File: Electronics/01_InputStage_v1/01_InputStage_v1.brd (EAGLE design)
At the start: 100 x 80 mm, 32 parts, among them J1 BARRIER_BLOCK-2PIN, J17 CONN_2X3_SMD, J2 BARRIER_BLOCK-2PIN, J3 BARRIER_BLOCK-2PIN, SW1 SWITCH_TABSSWITCH_TABS3, U1 XL4005-DEV, U2 DIODE_BIG

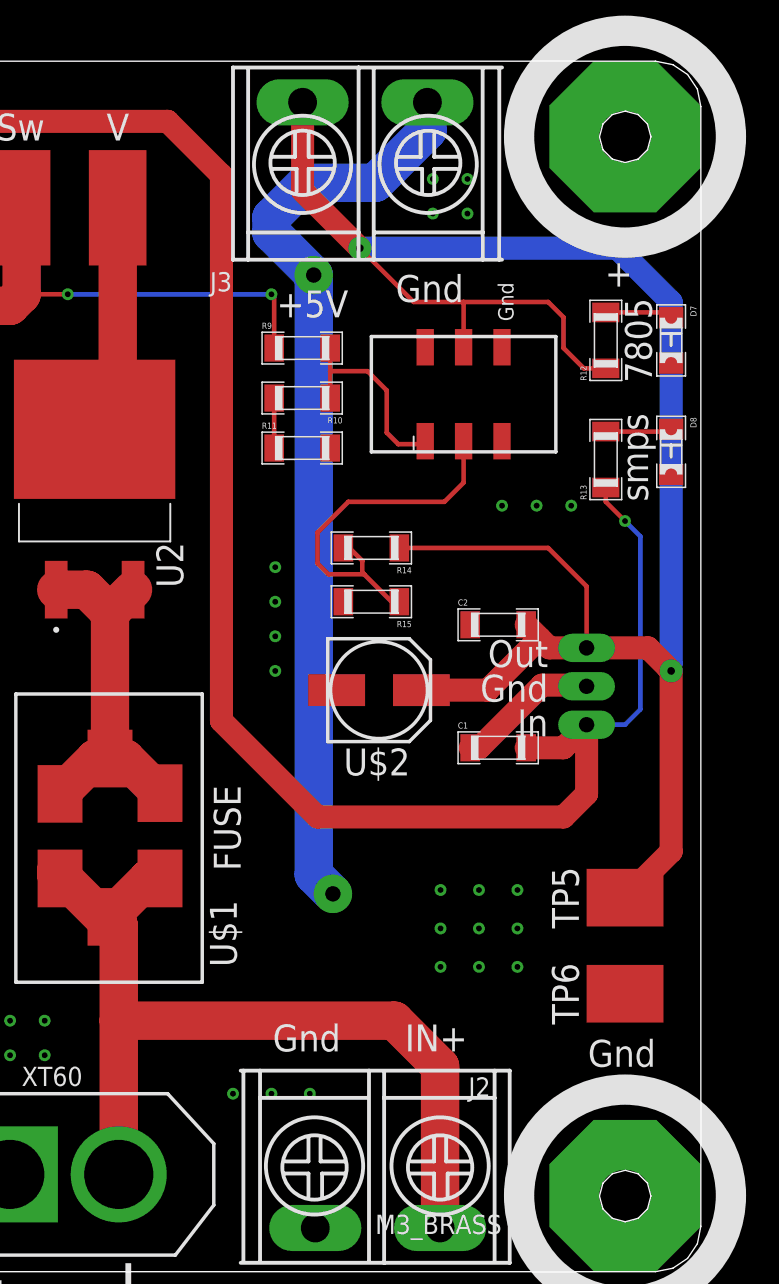
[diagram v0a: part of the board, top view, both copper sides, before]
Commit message: Input stage: Added PTC and moved some traces around
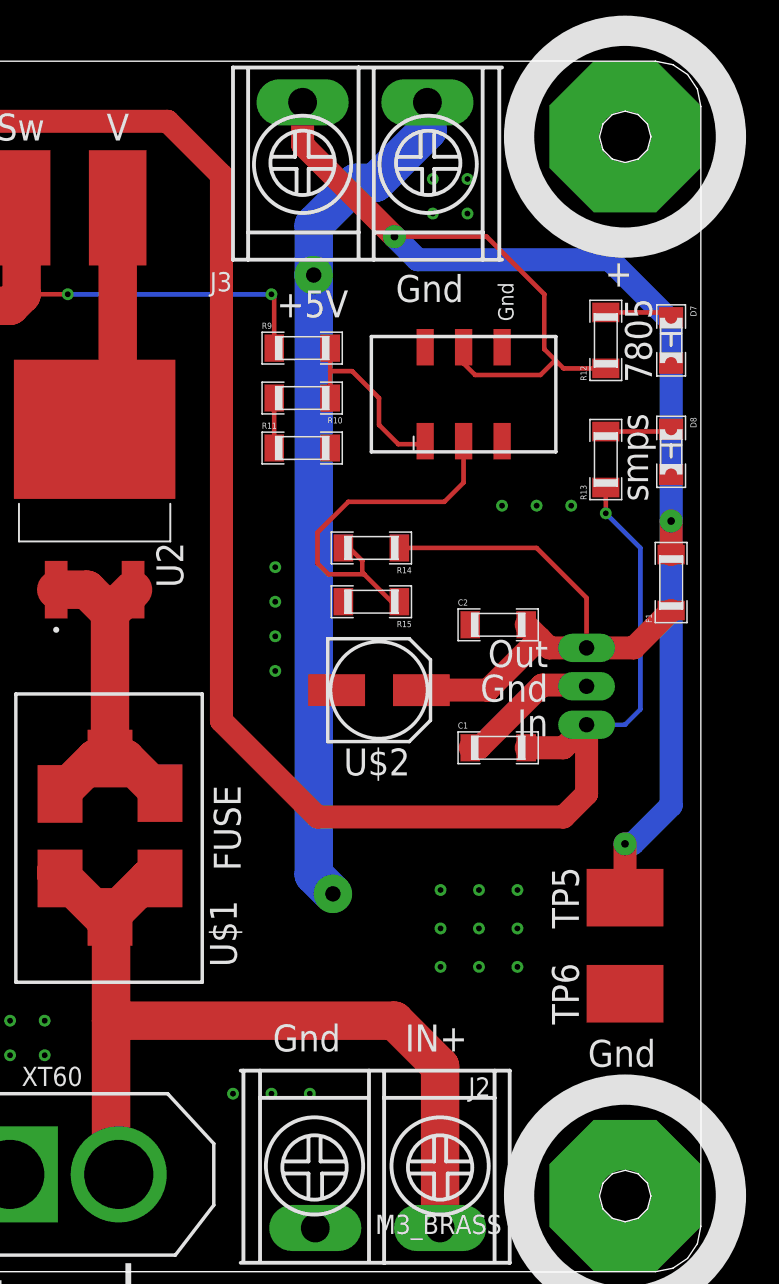
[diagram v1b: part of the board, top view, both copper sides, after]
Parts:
- added F1: PTCPTC_1206, Hippo-PS:1206
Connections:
- new net N: C2.2, F1.1, R14.1, U$2.+, U3.OUT
- net +5V: now also F1.2; no longer C2.2, R14.1, U$2.+, U3.OUT
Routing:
- net N: track 0.00 -> 37.5 mm
- net +5V: track 135.4 -> 101.4 mm, vias 2 -> 3
- net GND: track 98.6 -> 94.4 mm
- net IN+_SIG: track 13.3 -> 12.7 mm
- net IN+: track 60.2 -> 60.7 mm

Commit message: Change fuse holder to through-hole component
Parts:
- removed U$1: FUSE, Hippo-PS:FUSE
- added F2: FUSE_HOLDER_TH, Hippo-PS:FUSE_HOLDER_TH
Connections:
- net IN+: now also F2.1, F2.2; no longer U$1.P$1, U$1.P$2, U$1.P$3
- net N$1: now also F2.3, F2.4; no longer U$1.P$4, U$1.P$5, U$1.P$6
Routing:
- net N$1: track 24.5 -> 16.5 mm
- net IN+: track 60.7 -> 54.5 mm
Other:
- board text added: "hippo-pd input v1"
- board text removed: "hippo-ps input v1"
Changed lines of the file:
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@@
 <text x="156.972" y="46.99" size="1.524" layer="25" font="vector" ratio="15">word</text>
 <text x="104.902" y="81.026" size="1.016" layer="21" font="vector" ratio="14" rot="R90">Gnd</text>
-<text x="29.718" y="63.5" size="1.016" layer="21" font="vector" ratio="14" rot="R90">hippo-ps input v1</text>
-<text x="29.718" y="36.576" size="1.016" layer="21" font="vector" ratio="14" rot="R90">ek robotgrrl jul 10, `22</text>
+<text x="28.956" y="75.946" size="1.016" layer="21" font="vector" ratio="14" rot="SR270">hippo-pd input v1</text>
+<text x="28.702" y="52.832" size="1.016" layer="21" font="vector" ratio="14" rot="SR270">ek robotgrrl jul 10, `22</text>
 <text x="93.472" y="34.544" size="1.778" layer="21" font="vector" ratio="14" rot="R180">Gnd</text>
 <text x="101.854" y="34.544" size="1.778" layer="21" font="vector" ratio="14" rot="R180">IN+</text>
@@
 <attribute name="VALUE" x="72.39" y="30.48" size="1.27" layer="21" font="vector" ratio="14"/>
 </element>
-<element name="U$1" library="Hippo-PS" package="FUSE" value="FUSE" x="84.328" y="37.338" smashed="yes" rot="R90">
-<attribute name="NAME" x="86.614" y="38.354" size="1.778" layer="21" font="vector" ratio="14" rot="R90"/>
-<attribute name="VALUE" x="86.868" y="44.704" size="1.778" layer="21" font="vector" ratio="14" rot="R90"/>
-</element>
 <element name="TP1" library="Hippo-PS" package="TP" value="TP" x="34.798" y="36.322" smashed="yes">
 <attribute name="NAME" x="32.512" y="34.29" size="1.778" layer="25" font="vector" ratio="14" rot="R90"/>
@@
 <attribute name="VALUE" x="116.967" y="61.087" size="0.4064" layer="27" font="vector" rot="R90"/>
 </element>
+<element name="F2" library="Hippo-PS" package="FUSE_HOLDER_TH" value="FUSE_HOLDER_TH" x="75.438" y="41.91" smashed="yes" rot="R90">
+<attribute name="COPYRIGHT" value="Copyright (C) 2022 Ultra Librarian. All rights reserved." x="75.438" y="41.91" size="1.778" layer="27" rot="R90" display="off"/>
+<attribute name="DIGI-KEY_PART_NUMBER_1" value="36-3557-10-ND" x="75.438" y="41.91" size="1.778" layer="27" rot="R90" display="off"/>
+<attribute name="MANUFACTURER_PART_NUMBER" value="3557-10" x="75.438" y="41.91" size="1.778" layer="27" rot="R90" display="off"/>
+<attribute name="MFR_NAME" value="Keystone Electronics" x="75.438" y="41.91" size="1.778" layer="27" rot="R90" display="off"/>
+<attribute name="NAME" x="77.7748" y="45.3644" size="1.27" layer="27" ratio="6" rot="SR90"/>
+<attribute name="VALUE" x="77.5208" y="48.4378" size="1.27" layer="21" ratio="6" rot="SR90"/>
+</element>
 </elements>
 <signals>
@@
 <contactref element="U$5" pad="V+"/>
 <contactref element="J2" pad="P$1"/>
-<contactref element="U$1" pad="P$3"/>
-<contactref element="U$1" pad="P$2"/>
-<contactref element="U$1" pad="P$1"/>
-<wire x1="78.302" y1="34.798" x2="78.302" y2="25.146" width="2.54" layer="1"/>
+<wire x1="78.302" y1="25.146" x2="78.302" y2="34.798" width="2.54" layer="1"/>
 <wire x1="78.81" y1="24.638" x2="78.302" y2="25.146" width="2.54" layer="1"/>
-<wire x1="78.302" y1="34.798" x2="78.302" y2="41.586" width="2.54" layer="1"/>
-<wire x1="78.302" y1="41.586" x2="78.232" y2="41.656" width="2.54" layer="1"/>
-<wire x1="78.232" y1="41.656" x2="80.772" y2="44.196" width="2.54" layer="1"/>
-<wire x1="80.772" y1="44.196" x2="81.534" y2="44.196" width="2.54" layer="1"/>
-<wire x1="78.232" y1="41.656" x2="77.724" y2="41.656" width="2.54" layer="1"/>
-<wire x1="77.724" y1="41.656" x2="74.676" y2="44.704" width="2.54" layer="1"/>
-<wire x1="74.676" y1="44.704" x2="74.676" y2="44.45" width="2.54" layer="1"/>
-<wire x1="74.676" y1="44.45" x2="74.93" y2="44.196" width="2.54" layer="1"/>
 <wire x1="100.048" y1="21.096" x2="100.048" y2="31.778" width="2.54" layer="1"/>
 <wire x1="97.028" y1="34.798" x2="78.302" y2="34.798" width="2.54" layer="1"/>
 <wire x1="100.048" y1="31.778" x2="97.028" y2="34.798" width="2.54" layer="1"/>
+<contactref element="F2" pad="2"/>
+<contactref element="F2" pad="1"/>
+<wire x1="78.302" y1="34.798" x2="78.302" y2="41.3704" width="2.54" layer="1"/>
+<wire x1="78.302" y1="41.3704" x2="78.8416" y2="41.91" width="2.54" layer="1"/>
+<wire x1="75.438" y1="41.91" x2="77.7624" y2="41.91" width="2.54" layer="1"/>
+<wire x1="77.7624" y1="41.91" x2="78.302" y2="41.3704" width="2.54" layer="1"/>
 </signal>
 <signal name="GND">
@@
 </signal>
 <signal name="N$1">
-<contactref element="U$1" pad="P$4"/>
-<contactref element="U$1" pad="P$6"/>
-<contactref element="U$1" pad="P$5"/>
 <contactref element="U2" pad="3"/>
 <contactref element="U2" pad="1"/>
-<wire x1="74.93" y1="49.784" x2="77.2668" y2="52.1208" width="2.54" layer="1"/>
-<wire x1="77.2668" y1="52.1208" x2="78.232" y2="52.1208" width="2.54" layer="1"/>
-<wire x1="81.534" y1="49.8348" x2="79.248" y2="52.1208" width="2.54" layer="1"/>
-<wire x1="79.248" y1="52.1208" x2="78.232" y2="52.1208" width="2.54" layer="1"/>
-<wire x1="78.232" y1="52.1208" x2="78.232" y2="61.756" width="2.54" layer="1"/>
-<wire x1="78.232" y1="61.756" x2="79.756" y2="63.28" width="2.54" layer="1"/>
-<wire x1="78.232" y1="61.756" x2="76.708" y2="63.28" width="2.54" layer="1"/>
-<wire x1="76.708" y1="63.28" x2="74.676" y2="63.28" width="2.54" layer="1"/>
+<wire x1="79.756" y1="63.28" x2="77.216" y2="63.28" width="2.54" layer="1"/>
+<contactref element="F2" pad="3"/>
+<contactref element="F2" pad="4"/>
+<wire x1="77.216" y1="63.28" x2="74.676" y2="63.28" width="2.54" layer="1"/>
+<wire x1="75.438" y1="55.372" x2="76.962" y2="55.372" width="2.54" layer="1"/>
+<wire x1="76.962" y1="55.372" x2="78.8416" y2="55.372" width="2.54" layer="1"/>
+<wire x1="76.962" y1="55.372" x2="76.962" y2="63.026" width="2.54" layer="1"/>
+<wire x1="76.962" y1="63.026" x2="77.216" y2="63.28" width="2.54" layer="1"/>
 </signal>
 <signal name="V+">

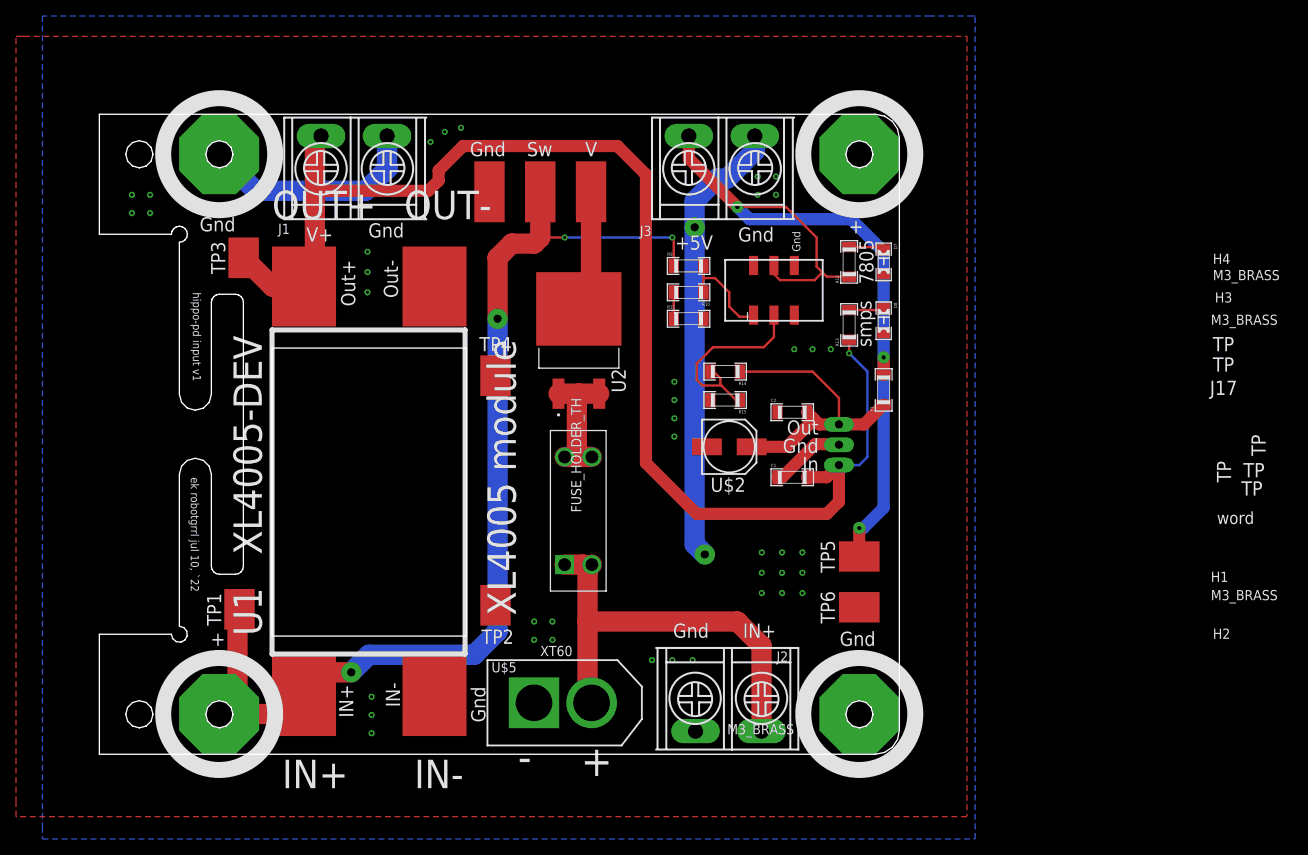
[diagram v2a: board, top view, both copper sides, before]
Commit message: Move LEDs to side on input stage
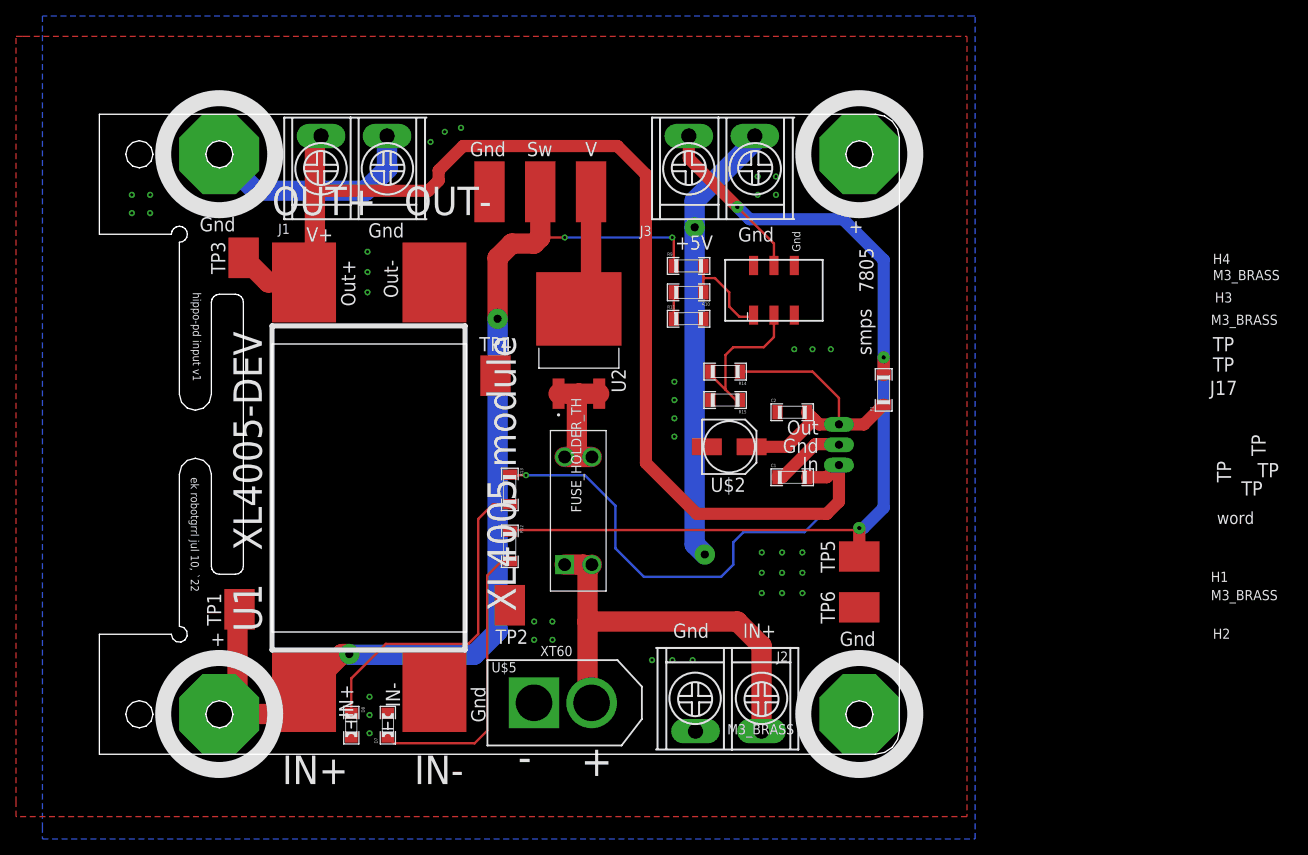
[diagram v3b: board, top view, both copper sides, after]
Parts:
- moved D7 84.8 mm to (53.3, 21.8), turned to 90 degrees
- moved D8 83.6 mm to (48.8, 21.8)
- moved R12 55.4 mm to (68.6, 44.2), turned to 270 degrees
- moved R13 47.1 mm to (68.6, 51.3), turned to 270 degrees
- moved TP2 1.78 mm to (68.6, 36.8)
- moved U1 0.51 mm to (38.9, 31.0)
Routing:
- net V+: track 169.7 -> 209.8 mm
- net N$5: track 4.38 -> 41.6 mm
- net N$6: track 4.46 -> 36.3 mm
- net +5V: track 101.4 -> 126.3 mm
- net +5V_SIG: track 24.8 -> 19.4 mm
- net SAFE_IN+: track 137.1 -> 134.9 mm
- net GND: track 94.4 -> 93.6 mm
